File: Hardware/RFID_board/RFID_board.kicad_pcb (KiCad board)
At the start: 2 copper layers, 13 parts, among them J1 Conn_01x08_Male, Q1 2N3904, U1 ID-3LA

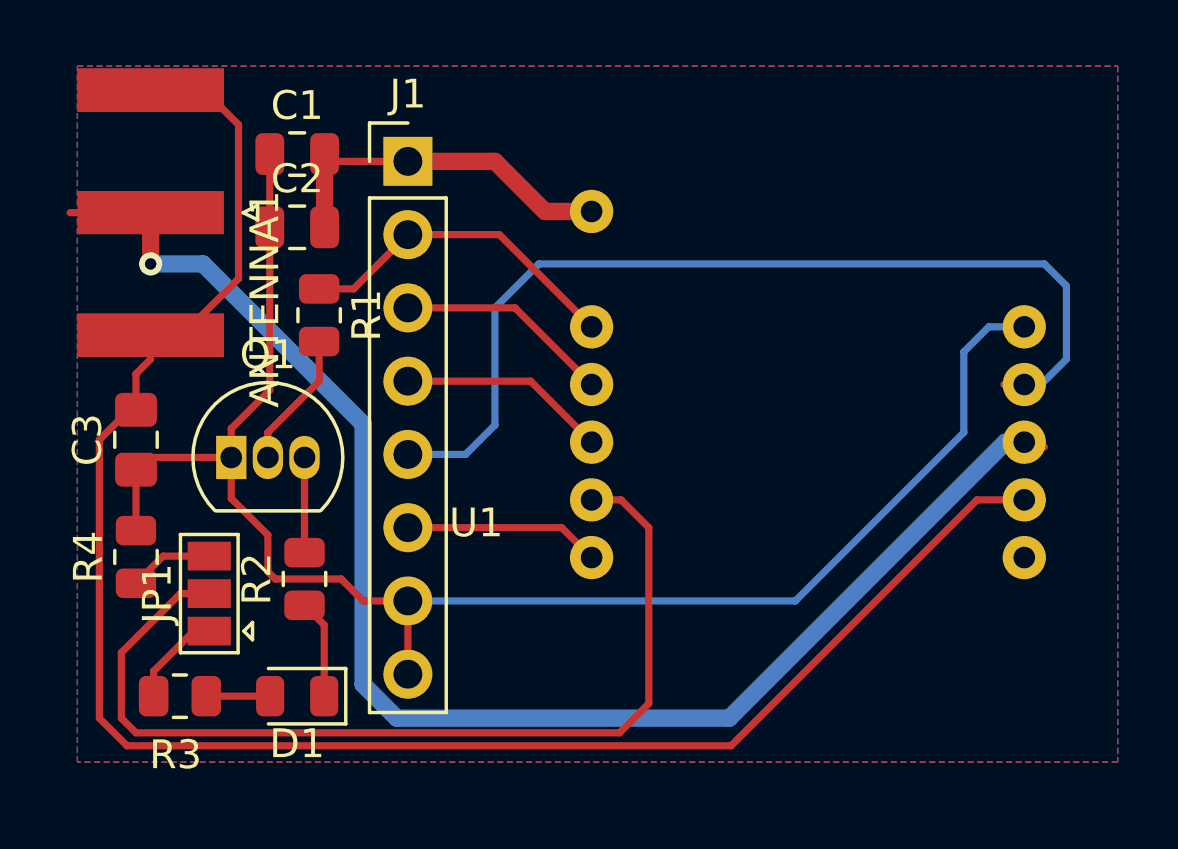
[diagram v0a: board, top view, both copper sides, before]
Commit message: all boards pass DRC and have appropriate silkscreens, will order tomorrow
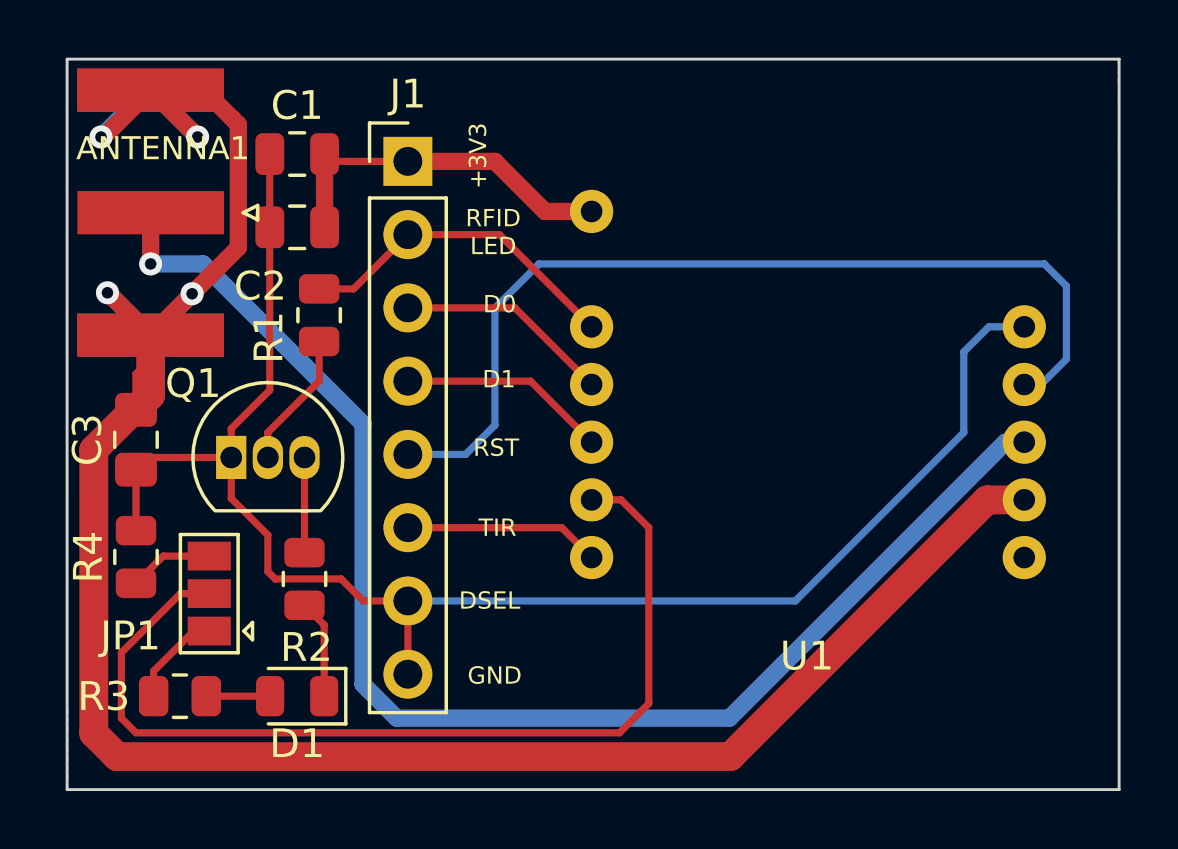
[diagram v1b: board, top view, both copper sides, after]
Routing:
- net Net-(ANTENNA1-Pad2): track 62.9 -> 79.0 mm, vias 0 -> 4
- net Net-(J1-Pad5): track 33.9 -> 32.0 mm
- net Net-(ANTENNA1-Pad1): track 49.4 -> 47.8 mm
- net GND: track 55.9 -> 55.3 mm
- net Net-(JP1-Pad1): track 3.37 -> 2.83 mm
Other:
- board outline added: 36.5 x 25.3 mm
- board text added: "+3V3"
- board text added: "D0"
- board text added: "D1"
- board text added: "DSEL"
- board text added: "GND"
- board text added: "RFID Board ECE445 SP22 Group 45 v0.0.1"
- board text added: "RFID LED"
- board text added: "RST"
- board text added: "TIR"
